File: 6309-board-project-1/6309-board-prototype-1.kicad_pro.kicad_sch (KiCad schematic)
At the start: 35 parts, among them J1 PWR, J2 FTDI, SW1 B3F-1000, U1 63C09, U2 62256, U3 39FS010, U4 16550, U5 74HCT04, U6 74HCT32, U7 74HCT30, X1 12MHz, X2 1.8432 MHz

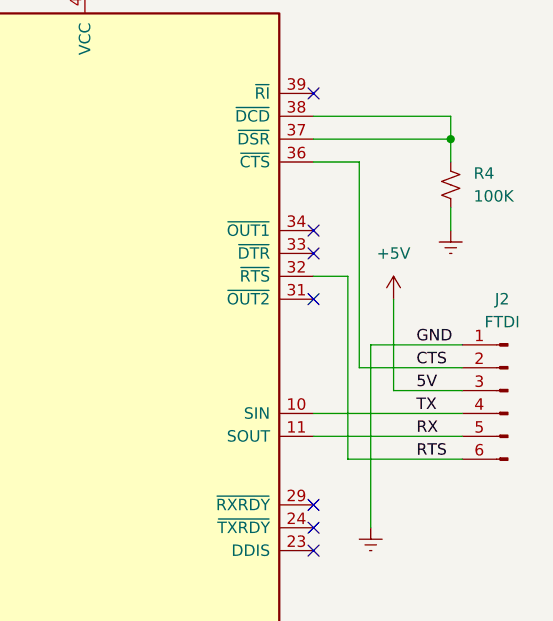
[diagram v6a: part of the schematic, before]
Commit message: fixed CTS/RTS and doubled width of power traces
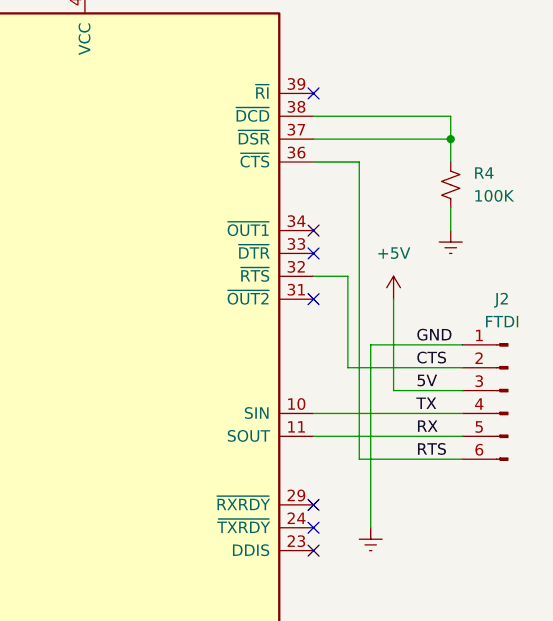
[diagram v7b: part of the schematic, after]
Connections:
- net CTS: now also U4.32 (~{RTS}); no longer U4.36 (~{CTS})
- net RTS: now also U4.36 (~{CTS}); no longer U4.32 (~{RTS})
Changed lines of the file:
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@@
 		)
 	)
-	(wire
-		(pts
-			(xy 265.43 96.52) (xy 265.43 73.66)
-		)
-		(stroke
-			(width 0)
-			(type default)
-		)
-	)
-	(wire
-		(pts
-			(xy 264.16 106.68) (xy 276.86 106.68)
-		)
-		(stroke
-			(width 0)
-			(type default)
-		)
-	)
 	(bus
 		(pts
@@
 		)
 	)
-	(wire
-		(pts
-			(xy 276.86 96.52) (xy 265.43 96.52)
-		)
-		(stroke
-			(width 0)
-			(type default)
-		)
-	)
 	(bus
 		(pts
@@
 		)
 	)
+	(wire
+		(pts
+			(xy 265.43 106.68) (xy 276.86 106.68)
+		)
+		(stroke
+			(width 0)
+			(type default)
+		)
+	)
 	(polyline
 		(pts
@@
 	(wire
 		(pts
+			(xy 264.16 86.36) (xy 264.16 96.52)
+		)
+		(stroke
+			(width 0)
+			(type default)
+		)
+	)
+	(wire
+		(pts
 			(xy 165.1 162.56) (xy 167.64 162.56)
 		)
@@
 	(wire
 		(pts
+			(xy 265.43 73.66) (xy 265.43 106.68)
+		)
+		(stroke
+			(width 0)
+			(type default)
+		)
+	)
+	(wire
+		(pts
 			(xy 196.85 101.6) (xy 209.55 101.6)
 		)
@@
 		)
 	)
-	(wire
-		(pts
-			(xy 264.16 86.36) (xy 264.16 106.68)
-		)
-		(stroke
-			(width 0)
-			(type default)
-		)
-	)
 	(bus
 		(pts
@@
 		)
 		(stroke
+			(width 0)
+			(type default)
+		)
+	)
+	(wire
+		(pts
+			(xy 264.16 96.52) (xy 276.86 96.52)
+		)
+		(stroke
